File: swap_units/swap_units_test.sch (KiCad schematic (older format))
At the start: 5 parts, among them U1 LM324, U2 PIC18F452-IP

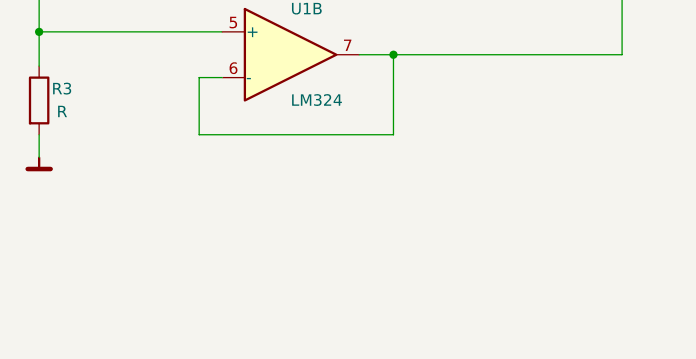
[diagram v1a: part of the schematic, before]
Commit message: Updated test project to include multiple hierarchy
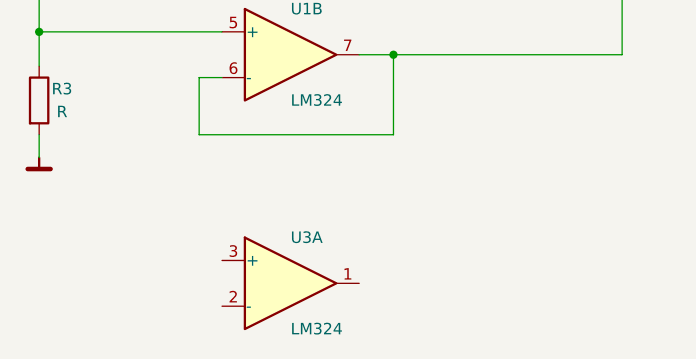
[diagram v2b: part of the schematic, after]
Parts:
- added U3: LM324, Package_DIP:DIP-14_W7.62mm, symbol Amplifier_Operational:LM324
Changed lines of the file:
@@
 $Descr A4 11693 8268
 encoding utf-8
-Sheet 1 3
+Sheet 1 4
 Title ""
 Date ""
@@
 Wire Wire Line
 	5700 3100 4750 3100
+$Comp
+L Amplifier_Operational:LM324 U3
+U 1 1 5C9CC657
+P 4300 6550
+F 0 "U3" H 4300 6750 50  0000 L CNN
+F 1 "LM324" H 4300 6350 50  0000 L CNN
+F 2 "Package_DIP:DIP-14_W7.62mm" H 4250 6650 50  0001 C CNN
+F 3 "http://www.ti.com/lit/ds/symlink/lm2902-n.pdf" H 4350 6750 50  0001 C CNN
+	1    4300 6550
+	1    0    0    -1
+$EndComp
 $EndSCHEMATC
